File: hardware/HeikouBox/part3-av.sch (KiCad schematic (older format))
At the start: 96 parts, among them J301 DB15_Female_HighDensity_Mount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, J302 AudioJack3_SwitchTR, Q301 MMBT3904, Q302 MMBT3904, Q303 MMBT3904, Q304 MMBT3904, Q305 MMBT3904, Q306 MMBT3904, Q307 MMBT3904

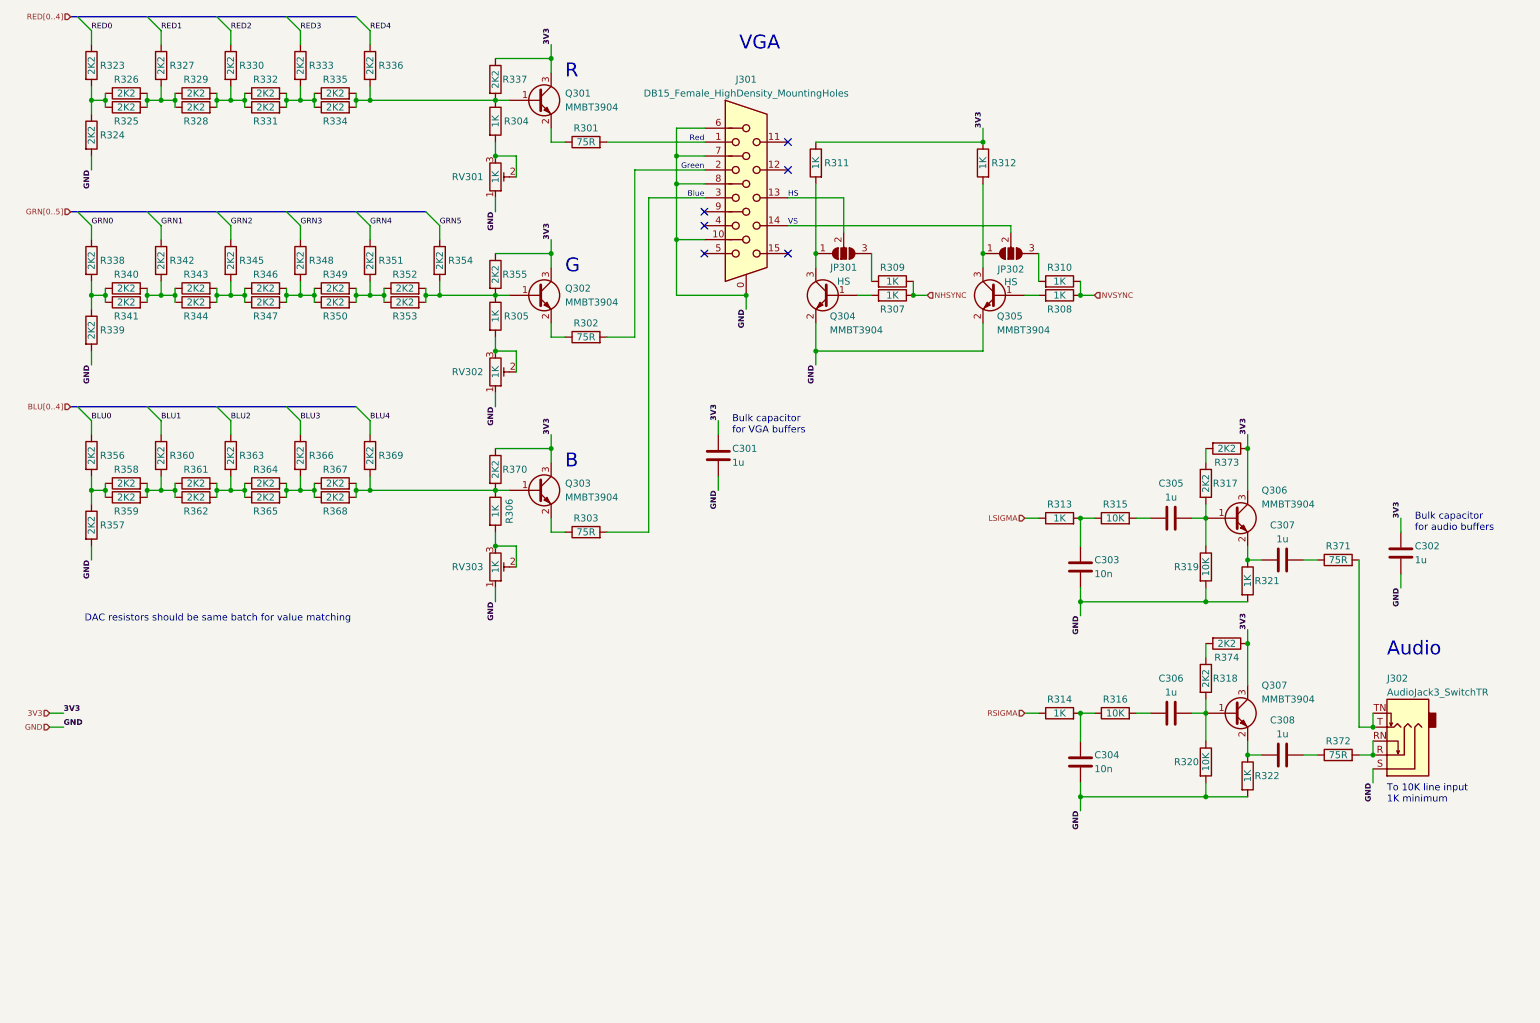
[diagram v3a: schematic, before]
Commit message: Cleanup routing
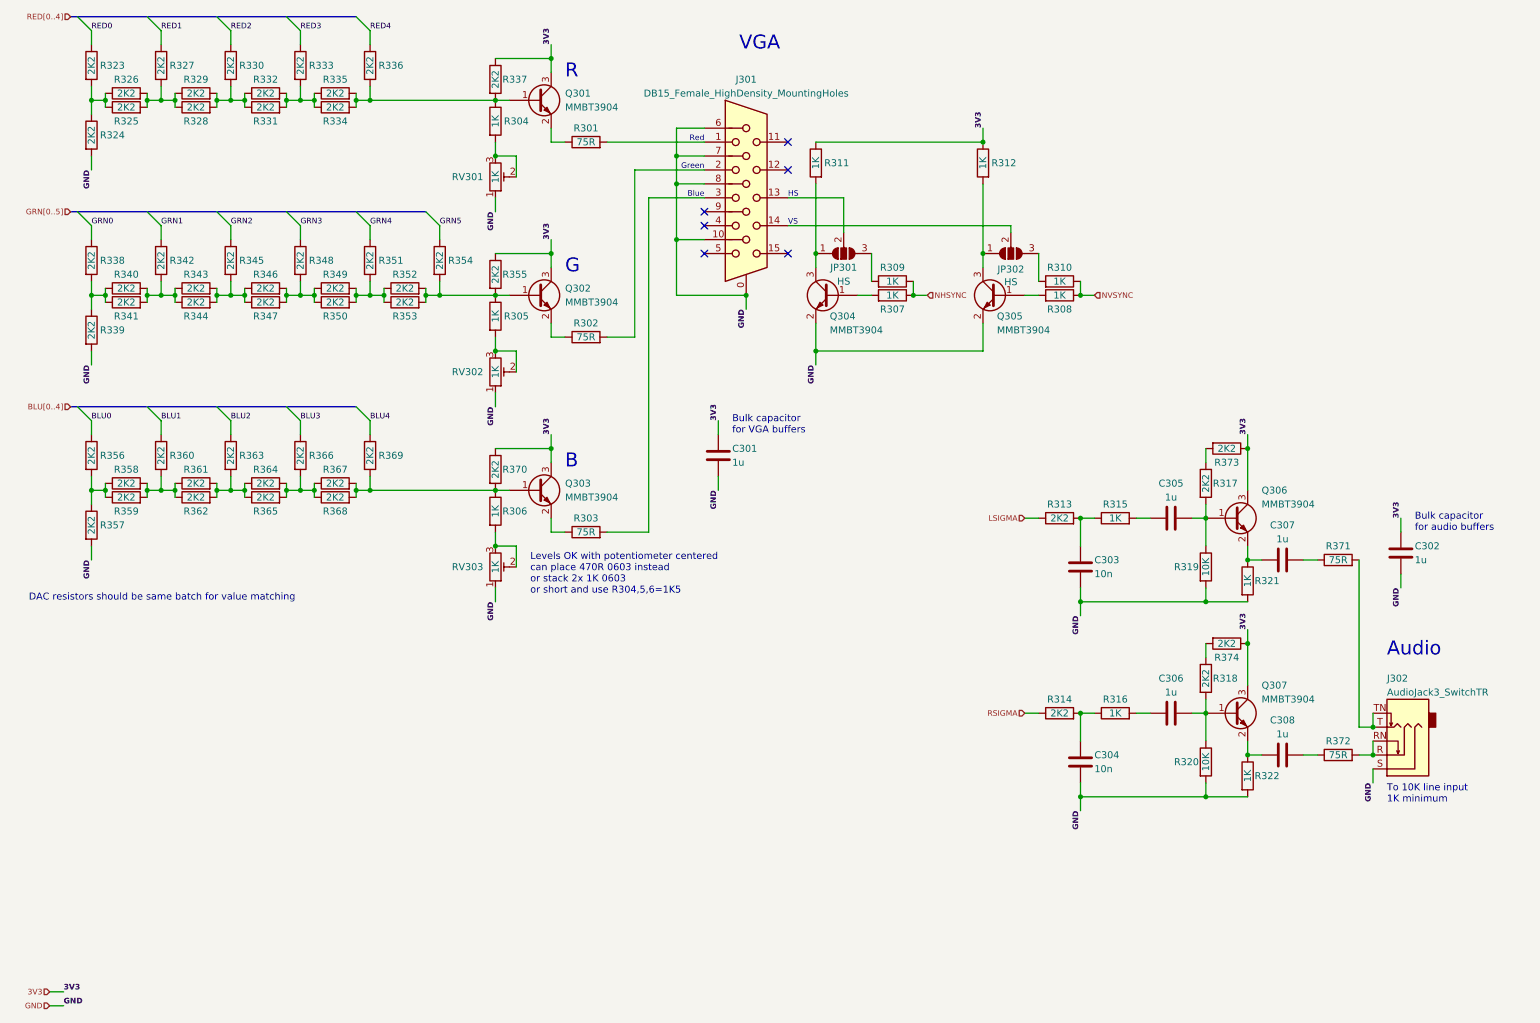
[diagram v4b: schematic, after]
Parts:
- R313, R314: value 1K -> 2K2
- R315, R316: value 10K -> 1K
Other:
- note added: "Levels OK with potentiometer centered\ncan place 470R 0603 instead\nor stack 2x 1K 0603\nor short and use R304,5,6=1K5"
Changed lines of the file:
@@
 Wire Wire Line
 	1000 700  1000 800
-$Comp
-L Transistor_BJT:MMBT3904 Q?
-U 1 1 610B6F8F
-P 4200 4000
-AR Path="/610B6F8F" Ref="Q?"  Part="1"
-AR Path="/62C73AC4/610B6F8F" Ref="Q303"  Part="1"
-F 0 "Q303" H 4400 4050 50  0000 L CNN
-F 1 "MMBT3904" H 4400 3950 50  0000 L CNN
-F 2 "Package_TO_SOT_SMD:SOT-23" H 4400 3925 50  0001 L CIN
-F 3 "https://www.fairchildsemi.com/datasheets/2N/2N3904.pdf" H 4200 4000 50  0001 L CNN
-	1    4200 4000
-	1    0    0    -1
-$EndComp
 Text HLabel 850  3400 0    40   Input ~ 0
 BLU[0..4]
@@
 	-1   0    0    -1
 $EndComp
-Text HLabel 700  5700 0    40   Input ~ 0
+Text HLabel 700  7700 0    40   Input ~ 0
 GND
 Wire Wire Line
@@
 	5500 4000 5500 3900
 Wire Wire Line
-	700  5700 800  5700
+	700  7700 800  7700
 Connection ~ 3900 1600
 Connection ~ 3900 4000
@@
 AR Path="/6328C84B" Ref="R?"  Part="1"
 AR Path="/62C73AC4/6328C84B" Ref="R306"  Part="1"
-F 0 "R306" V 4000 4150 50  0000 C CNN
+F 0 "R306" H 3950 4150 50  0000 L CNN
 F 1 "1K" V 3900 4150 50  0000 C CNN
 F 2 "Resistor_SMD:R_0603_1608Metric_Pad0.98x0.95mm_HandSolder" V 3830 4150 50  0001 C CNN
@@
 Wire Wire Line
 	3900 900  4300 900
-Text HLabel 700  5600 0    40   Input ~ 0
+Text HLabel 700  7600 0    40   Input ~ 0
 3V3
 Wire Wire Line
@@
 Wire Wire Line
 	4700 1500 5400 1500
-Text Notes 950  4950 0    50   ~ 0
+Text Notes 550  4800 0    50   ~ 0
 DAC resistors should be same batch for value matching
 $Comp
@@
 $Comp
 L Device:R R?
-U 1 1 62F010C1
-P 7950 5600
-AR Path="/62F010C1" Ref="R?"  Part="1"
-AR Path="/62C73AC4/62F010C1" Ref="R314"  Part="1"
-F 0 "R314" V 8050 5600 50  0000 C CNN
-F 1 "1K" V 7950 5600 50  0000 C CNN
-F 2 "Resistor_SMD:R_0603_1608Metric_Pad0.98x0.95mm_HandSolder" V 7880 5600 50  0001 C CNN
-F 3 "~" H 7950 5600 50  0001 C CNN
-	1    7950 5600
-	0    -1   -1   0
-$EndComp
-$Comp
-L Device:R R?
 U 1 1 62F01086
 P 8350 5600
@@
 AR Path="/62C73AC4/62F01086" Ref="R316"  Part="1"
 F 0 "R316" V 8450 5600 50  0000 C CNN
-F 1 "10K" V 8350 5600 50  0000 C CNN
+F 1 "1K" V 8350 5600 50  0000 C CNN
 F 2 "Resistor_SMD:R_0603_1608Metric_Pad0.98x0.95mm_HandSolder" V 8280 5600 50  0001 C CNN
 F 3 "~" H 8350 5600 50  0001 C CNN
@@
 $Comp
 L Device:R R?
-U 1 1 60742614
-P 7950 4200
-AR Path="/60742614" Ref="R?"  Part="1"
-AR Path="/62C73AC4/60742614" Ref="R313"  Part="1"
-F 0 "R313" V 8050 4200 50  0000 C CNN
-F 1 "1K" V 7950 4200 50  0000 C CNN
-F 2 "Resistor_SMD:R_0603_1608Metric_Pad0.98x0.95mm_HandSolder" V 7880 4200 50  0001 C CNN
-F 3 "~" H 7950 4200 50  0001 C CNN
-	1    7950 4200
-	0    -1   -1   0
-$EndComp
-$Comp
-L Device:R R?
 U 1 1 6074260E
 P 8350 4200
@@
 AR Path="/62C73AC4/6074260E" Ref="R315"  Part="1"
 F 0 "R315" V 8450 4200 50  0000 C CNN
-F 1 "10K" V 8350 4200 50  0000 C CNN
+F 1 "1K" V 8350 4200 50  0000 C CNN
 F 2 "Resistor_SMD:R_0603_1608Metric_Pad0.98x0.95mm_HandSolder" V 8280 4200 50  0001 C CNN
 F 3 "~" H 8350 4200 50  0001 C CNN
@@
 	3500 2600 3900 2600
 Connection ~ 3500 2600
-Text Label 800  5700 0    40   ~ 8
+Text Label 800  7700 0    40   ~ 8
 GND
 Wire Wire Line
@@
 Wire Wire Line
 	4300 800  4300 900
-Text Label 800  5600 0    40   ~ 8
+Text Label 800  7600 0    40   ~ 8
 3V3
 Wire Wire Line
-	700  5600 800  5600
+	700  7600 800  7600
 Text Label 5500 3500 1    40   ~ 8
 3V3
@@
 Text HLabel 8200 2600 2    40   Input ~ 0
 NVSYNC
-Wire Bus Line
-	850  2000 3400 2000
+Wire Wire Line
+	7000 2600 6900 2600
+Text HLabel 7000 2600 2    40   Input ~ 0
+NHSYNC
+Text Notes 4150 4750 0    50   ~ 0
+Levels OK with potentiometer centered\ncan place 470R 0603 instead\nor stack 2x 1K 0603\nor short and use R304,5,6=1K5
+$Comp
+L Transistor_BJT:MMBT3904 Q?
+U 1 1 610B6F8F
+P 4200 4000
+AR Path="/610B6F8F" Ref="Q?"  Part="1"
+AR Path="/62C73AC4/610B6F8F" Ref="Q303"  Part="1"
+F 0 "Q303" H 4400 4050 50  0000 L CNN
+F 1 "MMBT3904" H 4400 3950 50  0000 L CNN
+F 2 "Package_TO_SOT_SMD:SOT-23" H 4400 3925 50  0001 L CIN
+F 3 "https://www.fairchildsemi.com/datasheets/2N/2N3904.pdf" H 4200 4000 50  0001 L CNN
+	1    4200 4000
+	1    0    0    -1
+$EndComp
+$Comp
+L Device:R R?
+U 1 1 62F010C1
+P 7950 5600
+AR Path="/62F010C1" Ref="R?"  Part="1"
+AR Path="/62C73AC4/62F010C1" Ref="R314"  Part="1"
+F 0 "R314" V 8050 5600 50  0000 C CNN
+F 1 "2K2" V 7950 5600 50  0000 C CNN
+F 2 "Resistor_SMD:R_0603_1608Metric_Pad0.98x0.95mm_HandSolder" V 7880 5600 50  0001 C CNN
+F 3 "~" H 7950 5600 50  0001 C CNN
+	1    7950 5600
+	0    -1   -1   0
+$EndComp
+$Comp
+L Device:R R?
+U 1 1 60742614
+P 7950 4200
+AR Path="/60742614" Ref="R?"  Part="1"
+AR Path="/62C73AC4/60742614" Ref="R313"  Part="1"
+F 0 "R313" V 8050 4200 50  0000 C CNN
+F 1 "2K2" V 7950 4200 50  0000 C CNN
+F 2 "Resistor_SMD:R_0603_1608Metric_Pad0.98x0.95mm_HandSolder" V 7880 4200 50  0001 C CNN
+F 3 "~" H 7950 4200 50  0001 C CNN
+	1    7950 4200
+	0    -1   -1   0
+$EndComp
 Wire Bus Line
 	850  3400 2900 3400
 Wire Bus Line
 	850  600  2900 600
-Wire Wire Line
-	7000 2600 6900 2600
-Text HLabel 7000 2600 2    40   Input ~ 0
-NHSYNC
+Wire Bus Line
+	850  2000 3400 2000
 $EndSCHEMATC
